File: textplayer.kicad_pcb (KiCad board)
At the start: 2 copper layers, 46 parts, among them J1 ISP, J2 EXT, J3 SERIAL, J4 JTAG, SW1 SW_SPST, SW2 SW_SPST, SW3 SW_SPST, SW4 SW_SPST, SW5 SW_SPST, SW6 SW_SPST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

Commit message: placing...
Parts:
- moved R13 118.4 mm to (51.8, 46.1), turned to 90 degrees
- moved R12 98.6 mm to (51.6, 52.4), turned to 270 degrees
- moved R2 94.6 mm to (80.0, 33.6), turned to 270 degrees
- moved R1 94.5 mm to (82.3, 44.5)
- moved R11 93.8 mm to (52.0, 66.9), turned to 270 degrees
- moved C10 93.4 mm to (57.0, 65.5), turned to 180 degrees
- moved C3 88.9 mm to (68.5, 48.8), turned to 270 degrees
- moved SW6 79.4 mm to (127.5, 64.2)
- moved SW3 69.0 mm to (100.5, 73.2)
- moved R3 65.7 mm to (98.2, 56.6), turned to 270 degrees
- moved SW4 60.8 mm to (117.5, 73.3)
- moved R17 58.6 mm to (57.3, 39.5), turned to 270 degrees
- moved SW1 57.3 mm to (109.1, 64.5)
- moved SW2 56.1 mm to (109.3, 82.7)
- moved R16 55.6 mm to (60.8, 39.5), turned to 270 degrees
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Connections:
- U6 pad 48: (no net) -> +3V3
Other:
- board outline added: 100 x 70 mm

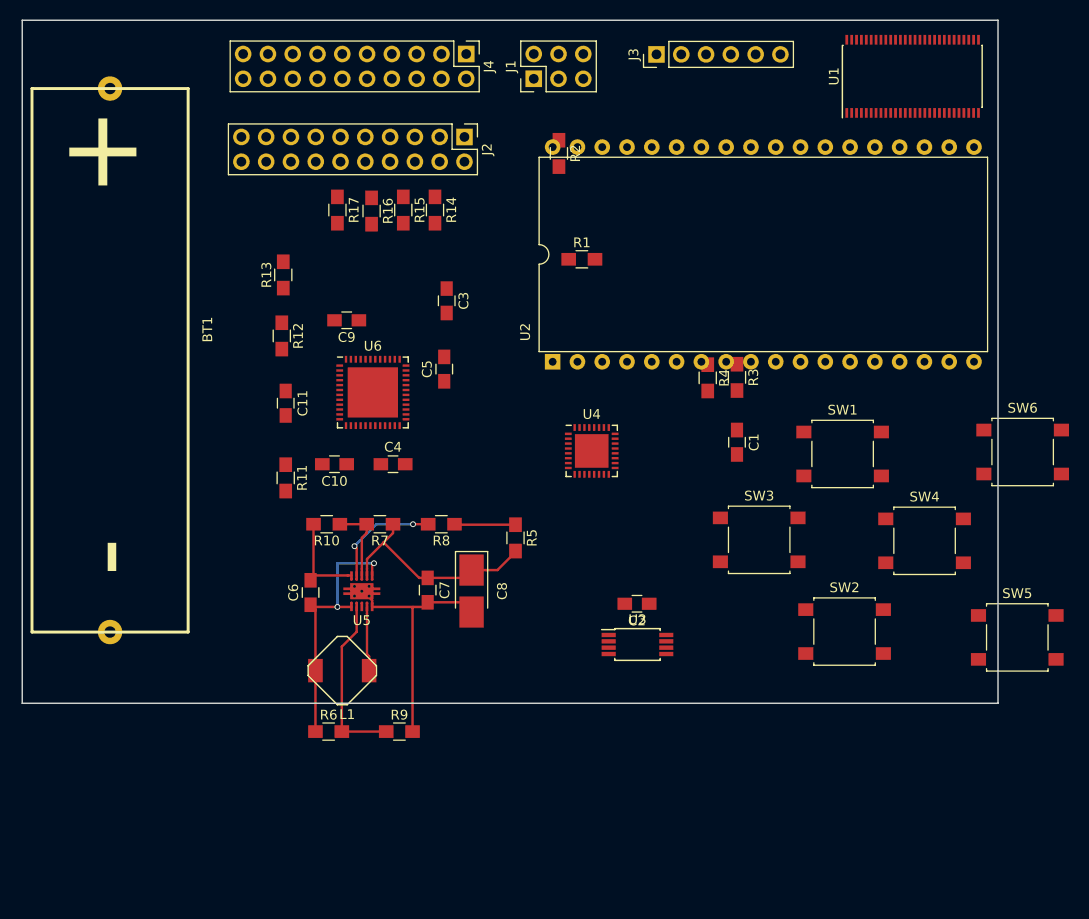
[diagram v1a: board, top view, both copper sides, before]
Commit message: displays schematic ausgelagert
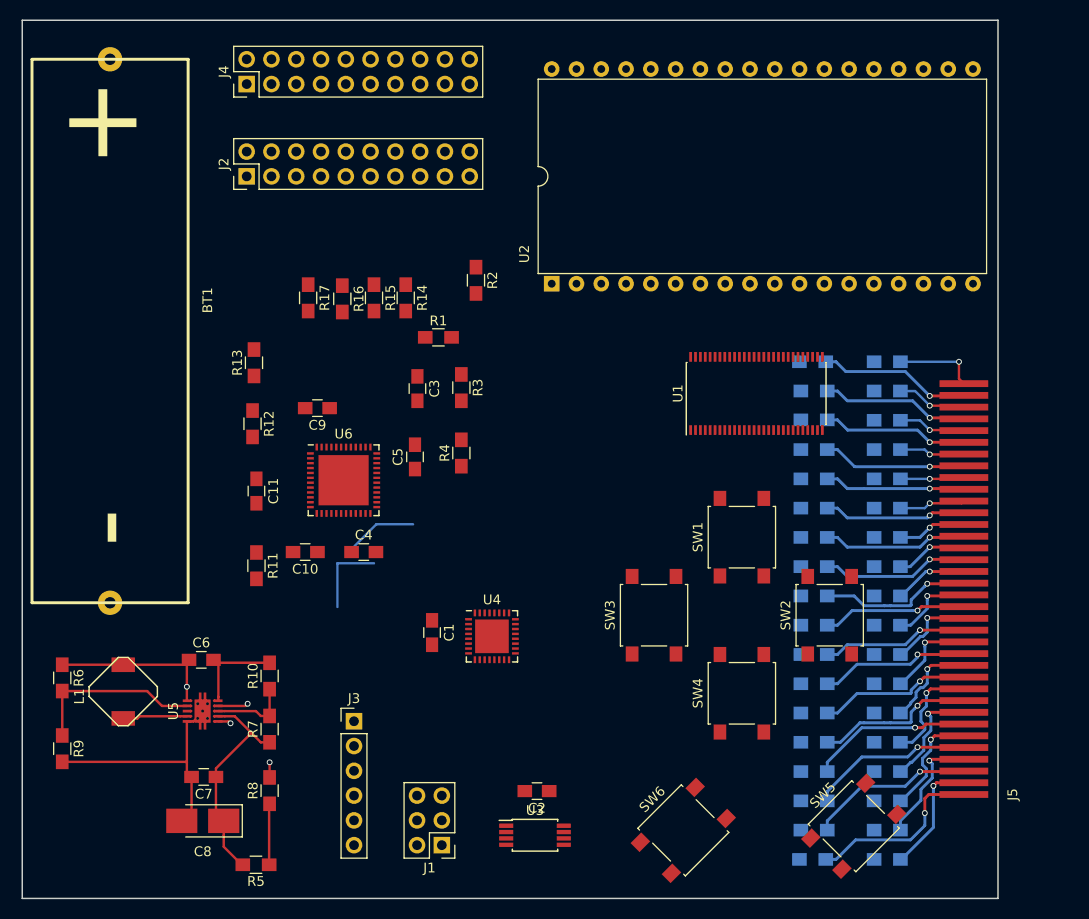
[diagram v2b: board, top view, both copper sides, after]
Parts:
- added J5: TI-30-LCD, Morn_SMD:TI-30-LCD, F.Cu at (121.5, 99.3)
- added R18: DNP, Resistors_SMD:R_0805_HandSoldering, B.Cu at (106.0, 106.0)
- added R19: DNP, Resistors_SMD:R_0805_HandSoldering, B.Cu at (113.7, 106.0)
- added R20: DNP, Resistors_SMD:R_0805_HandSoldering, B.Cu at (106.2, 103.0)
- added R21: DNP, Resistors_SMD:R_0805_HandSoldering, B.Cu at (113.7, 103.0)
- added R22: DNP, Resistors_SMD:R_0805_HandSoldering, B.Cu at (106.2, 100.0)
- added R23: DNP, Resistors_SMD:R_0805_HandSoldering, B.Cu at (113.7, 100.0)
- added R24: DNP, Resistors_SMD:R_0805_HandSoldering, B.Cu at (106.2, 97.0)
- added R25: DNP, Resistors_SMD:R_0805_HandSoldering, B.Cu at (113.7, 97.0)
- added R26: DNP, Resistors_SMD:R_0805_HandSoldering, B.Cu at (106.2, 94.0)
- added R27: DNP, Resistors_SMD:R_0805_HandSoldering, B.Cu at (113.7, 94.0)
- added R28: DNP, Resistors_SMD:R_0805_HandSoldering, B.Cu at (106.2, 91.0)
- added R29: DNP, Resistors_SMD:R_0805_HandSoldering, B.Cu at (113.7, 91.0)
- added R30: DNP, Resistors_SMD:R_0805_HandSoldering, B.Cu at (106.2, 88.0)
- added R31: DNP, Resistors_SMD:R_0805_HandSoldering, B.Cu at (113.7, 88.0)
- added R32: DNP, Resistors_SMD:R_0805_HandSoldering, B.Cu at (106.2, 85.0)
- added R33: DNP, Resistors_SMD:R_0805_HandSoldering, B.Cu at (113.7, 85.0)
- added R34: DNP, Resistors_SMD:R_0805_HandSoldering, B.Cu at (106.2, 82.0)
- added R35: DNP, Resistors_SMD:R_0805_HandSoldering, B.Cu at (113.7, 82.0)
- added R36: DNP, Resistors_SMD:R_0805_HandSoldering, B.Cu at (106.2, 79.0)
- added R37: DNP, Resistors_SMD:R_0805_HandSoldering, B.Cu at (113.7, 79.0)
- added R38: DNP, Resistors_SMD:R_0805_HandSoldering, B.Cu at (106.2, 76.0)
- added R39: DNP, Resistors_SMD:R_0805_HandSoldering, B.Cu at (113.7, 76.0)
- added R40: DNP, Resistors_SMD:R_0805_HandSoldering, B.Cu at (106.2, 73.0)
- added R41: DNP, Resistors_SMD:R_0805_HandSoldering, B.Cu at (113.7, 73.0)
- added R42: DNP, Resistors_SMD:R_0805_HandSoldering, B.Cu at (106.2, 70.0)
- added R43: DNP, Resistors_SMD:R_0805_HandSoldering, B.Cu at (113.7, 70.0)
- added R44: DNP, Resistors_SMD:R_0805_HandSoldering, B.Cu at (106.2, 67.0)
- added R45: DNP, Resistors_SMD:R_0805_HandSoldering, B.Cu at (113.7, 67.0)
- added R46: DNP, Resistors_SMD:R_0805_HandSoldering, B.Cu at (106.2, 64.0)
- added R47: DNP, Resistors_SMD:R_0805_HandSoldering, B.Cu at (113.7, 64.0)
- added R48: DNP, Resistors_SMD:R_0805_HandSoldering, B.Cu at (106.2, 61.0)
- added R49: DNP, Resistors_SMD:R_0805_HandSoldering, B.Cu at (113.7, 61.0)
- added R50: DNP, Resistors_SMD:R_0805_HandSoldering, B.Cu at (106.2, 58.0)
- added R51: DNP, Resistors_SMD:R_0805_HandSoldering, B.Cu at (113.7, 58.0)
- added R52: DNP, Resistors_SMD:R_0805_HandSoldering, B.Cu at (106.0, 55.0)
- added R53: DNP, Resistors_SMD:R_0805_HandSoldering, B.Cu at (113.7, 55.0)
- moved J1 79.1 mm to (68.0, 104.5), turned to 180 degrees
- moved J3 75.0 mm to (59.0, 91.8), turned to 0 degrees
- moved SW6 52.1 mm to (92.8, 103.0), turned to 45 degrees
- moved R5 42.8 mm to (49.0, 106.5), turned to 180 degrees
- moved C1 36.8 mm to (67.0, 82.8)
- moved C8 36.2 mm to (43.5, 102.0), turned to 180 degrees
- moved U1 36.2 mm to (100.2, 58.2)
- moved R9 34.6 mm to (29.1, 94.7), turned to 270 degrees
- moved R8 32.5 mm to (50.4, 99.0), turned to 90 degrees
- moved C7 29.9 mm to (43.6, 97.5), turned to 180 degrees
- moved R3 28.3 mm to (70.0, 57.6)
- moved R6 27.8 mm to (29.1, 87.4), turned to 270 degrees
- moved R4 26.4 mm to (70.0, 64.3), turned to 90 degrees
- moved SW5 25.6 mm to (110.2, 102.6), turned to 45 degrees
- moved SW4 24.4 mm to (98.8, 89.0), turned to 90 degrees
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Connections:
- net /BP0 renamed /Displays/BP0
- net /BP1 renamed /Displays/BP1
- net /BP2 renamed /Displays/BP2
- net /BP3 renamed /Displays/BP3
- J1 pad 5: /RESET -> /AVR_RESET
- U4 pad 11: /RESET -> /AVR_RESET
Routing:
- net Net-(J5-Pad1): track 0.00 -> 18.5 mm, vias 0 -> 1
- net Net-(J5-Pad3): track 0.00 -> 17.1 mm, vias 0 -> 1
- net Net-(J5-Pad5): track 0.00 -> 16.8 mm, vias 0 -> 1
- net Net-(J5-Pad7): track 0.00 -> 16.6 mm, vias 0 -> 1
- net Net-(J5-Pad9): track 0.00 -> 16.4 mm, vias 0 -> 1
- net Net-(J5-Pad11): track 0.00 -> 15.7 mm, vias 0 -> 1
- net Net-(J5-Pad19): track 0.00 -> 15.7 mm, vias 0 -> 1
- net Net-(J5-Pad35): track 0.00 -> 15.6 mm, vias 0 -> 1
- net Net-(J5-Pad13): track 0.00 -> 15.4 mm, vias 0 -> 1
- net Net-(J5-Pad33): track 0.00 -> 15.2 mm, vias 0 -> 1
- net Net-(J5-Pad21): track 0.00 -> 15.2 mm, vias 0 -> 1
- net Net-(J5-Pad15): track 0.00 -> 15.0 mm, vias 0 -> 1
- net Net-(J5-Pad31): track 0.00 -> 15.0 mm, vias 0 -> 1
- net Net-(J5-Pad23): track 0.00 -> 14.9 mm, vias 0 -> 1
- net Net-(J5-Pad17): track 0.00 -> 14.8 mm, vias 0 -> 1
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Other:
- board size 100 x 70 mm -> 100 x 90 mm

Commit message: place should be done now
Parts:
- added J10: GND, Measurement_Points:Measurement_Point_Round-TH_Small, F.Cu at (62.0, 102.0)
- added J11: GND, Measurement_Points:Measurement_Point_Round-SMD-Pad_Big, F.Cu at (62.0, 107.0)
- added J12: VCC, Measurement_Points:Measurement_Point_Round-TH_Small, F.Cu at (55.0, 102.0)
- added J13: VCC, Measurement_Points:Measurement_Point_Round-SMD-Pad_Big, F.Cu at (55.0, 107.0)
- added J6: BP0, Measurement_Points:Measurement_Point_Square-SMD-Pad_Small, B.Cu at (99.0, 57.8)
- added J7: BP2, Measurement_Points:Measurement_Point_Square-SMD-Pad_Small, B.Cu at (99.0, 54.8)
- added J8: BP1, Measurement_Points:Measurement_Point_Square-SMD-Pad_Small, B.Cu at (99.0, 60.8)
- added J9: BP3, Measurement_Points:Measurement_Point_Square-SMD-Pad_Small, B.Cu at (99.0, 63.8)
- moved BT1 53.6 mm to (35.1, 26.1), turned to 270 degrees
- moved R2 40.6 mm to (78.2, 86.8), turned to 180 degrees
- moved R3 33.4 mm to (78.2, 90.0), turned to 180 degrees
- moved R1 32.7 mm to (78.2, 83.5)
- moved R4 30.3 mm to (78.2, 93.5), turned to 180 degrees
- moved C1 27.6 mm to (90.0, 67.5), turned to 0 degrees
- moved R11 27.6 mm to (48.0, 48.4)
- moved R12 26.8 mm to (72.0, 48.4)
- moved C3 25.6 mm to (78.2, 80.0), turned to 0 degrees
- moved U1 13.4 mm to (86.9, 59.8), turned to 270 degrees
- moved U4 9.85 mm to (74.4, 73.4)
- moved J1 8.68 mm to (69.5, 96.0)
- moved J3 8.60 mm to (60.0, 83.3)
- moved R13 7.49 mm to (52.0, 48.4)
- moved R15 6.95 mm to (68.0, 48.4)
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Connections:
- R1 pad 2: Net-(R1-Pad2) -> /SDA
- U1 pad 10: Net-(U1-Pad10) -> /Displays/5L
- U1 pad 11: Net-(U1-Pad11) -> /Displays/5E
- U1 pad 13: Net-(U1-Pad13) -> /Displays/8D
- U1 pad 14: Net-(U1-Pad14) -> /Displays/8M
- U1 pad 15: Net-(U1-Pad15) -> /Displays/7D
- U1 pad 16: Net-(U1-Pad16) -> /Displays/7M
- U1 pad 17: Net-(U1-Pad17) -> /Displays/6D
- U1 pad 18: Net-(U1-Pad18) -> /Displays/6M
- U1 pad 19: Net-(U1-Pad19) -> /Displays/5D
- U1 pad 20: Net-(U1-Pad20) -> /Displays/5M
- U1 pad 21: Net-(U1-Pad21) -> /Displays/4D
- U1 pad 22: Net-(U1-Pad22) -> /Displays/4M
- U1 pad 23: Net-(U1-Pad23) -> /Displays/3D
- U1 pad 24: Net-(U1-Pad24) -> /Displays/3M
- U1 pad 25: Net-(U1-Pad25) -> /Displays/2D
- U1 pad 26: Net-(U1-Pad26) -> /Displays/2M
- U1 pad 27: Net-(U1-Pad27) -> /Displays/1D
- U1 pad 28: Net-(U1-Pad28) -> /Displays/1M
- U1 pad 29: Net-(U1-Pad29) -> /Displays/1E
- U1 pad 30: Net-(U1-Pad30) -> /Displays/1L
- U1 pad 31: Net-(U1-Pad31) -> /Displays/2E
- U1 pad 32: Net-(U1-Pad32) -> /Displays/2L
- U1 pad 33: Net-(U1-Pad33) -> /Displays/3E
- U1 pad 34: Net-(U1-Pad34) -> /Displays/3L
- U1 pad 35: Net-(U1-Pad35) -> /Displays/4E
- U1 pad 36: Net-(U1-Pad36) -> /Displays/4L
- U1 pad 4: Net-(U1-Pad4) -> /Displays/8L
- U1 pad 5: Net-(U1-Pad5) -> /Displays/8E
- U1 pad 6: Net-(U1-Pad6) -> /Displays/7L
- U1 pad 7: Net-(U1-Pad7) -> /Displays/7E
- U1 pad 8: Net-(U1-Pad8) -> /Displays/6L
- U1 pad 9: Net-(U1-Pad9) -> /Displays/6E
- U2 pad 1: Net-(U2-Pad1) -> /Displays/1E
- U2 pad 10: Net-(U2-Pad10) -> /Displays/5L
- U2 pad 11: Net-(U2-Pad11) -> /Displays/6E
- U2 pad 12: Net-(U2-Pad12) -> /Displays/6L
- U2 pad 13: Net-(U2-Pad13) -> /Displays/7E
- U2 pad 14: Net-(U2-Pad14) -> /Displays/7L
- U2 pad 15: Net-(U2-Pad15) -> /Displays/8E
- U2 pad 16: Net-(U2-Pad16) -> /Displays/8L
- U2 pad 2: Net-(U2-Pad2) -> /Displays/1L
- U2 pad 21: Net-(U2-Pad21) -> /Displays/8D
- U2 pad 22: Net-(U2-Pad22) -> /Displays/8M
- U2 pad 23: Net-(U2-Pad23) -> /Displays/7D
- U2 pad 24: Net-(U2-Pad24) -> /Displays/7M
- U2 pad 25: Net-(U2-Pad25) -> /Displays/6D
- U2 pad 26: Net-(U2-Pad26) -> /Displays/6M
- U2 pad 27: Net-(U2-Pad27) -> /Displays/5D
- U2 pad 28: Net-(U2-Pad28) -> /Displays/5M
- U2 pad 29: Net-(U2-Pad29) -> /Displays/4D
- U2 pad 3: Net-(U2-Pad3) -> /Displays/2E
- U2 pad 30: Net-(U2-Pad30) -> /Displays/4M
- U2 pad 31: Net-(U2-Pad31) -> /Displays/3D
- U2 pad 32: Net-(U2-Pad32) -> /Displays/3M
- U2 pad 33: Net-(U2-Pad33) -> /Displays/2D
- U2 pad 34: Net-(U2-Pad34) -> /Displays/2M
- U2 pad 35: Net-(U2-Pad35) -> /Displays/1D
- U2 pad 36: Net-(U2-Pad36) -> /Displays/1M
- U2 pad 4: Net-(U2-Pad4) -> /Displays/2L
- U2 pad 5: Net-(U2-Pad5) -> /Displays/3E
- U2 pad 6: Net-(U2-Pad6) -> /Displays/3L
- U2 pad 7: Net-(U2-Pad7) -> /Displays/4E
- U2 pad 8: Net-(U2-Pad8) -> /Displays/4L
- U2 pad 9: Net-(U2-Pad9) -> /Displays/5E
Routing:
- net +3V3: track 6.27 -> 99.3 mm
- net GND: track 35.5 -> 95.2 mm
- net /Displays/8D: track 0.00 -> 53.4 mm
- net /Displays/BP2: track 0.00 -> 51.7 mm
- net /Displays/8M: track 0.00 -> 51.5 mm
- net /Displays/BP3: track 0.00 -> 50.3 mm
- net /Displays/7D: track 0.00 -> 49.5 mm
- net /Displays/7M: track 0.00 -> 47.5 mm
- net /Displays/6D: track 0.00 -> 45.6 mm
- net /Displays/6M: track 0.00 -> 43.6 mm
- net /Displays/5D: track 0.00 -> 41.7 mm
- net /Displays/5M: track 0.00 -> 39.7 mm
- net /Displays/4D: track 0.00 -> 37.7 mm
- net /Displays/4M: track 0.00 -> 35.8 mm
- net /Displays/3D: track 0.00 -> 34.9 mm
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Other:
- outline, holes or cut-outs redrawn

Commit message: routing...
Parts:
- moved C9 1.75 mm to (55.2, 58.0)
- moved C5 1.50 mm to (67.2, 64.8)
- turned U4 to 90 degrees
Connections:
- R18 pad 2: Net-(R18-Pad2) -> /Displays/1L
- R19 pad 2: Net-(R19-Pad2) -> /Displays/1E
- R20 pad 2: Net-(R20-Pad2) -> /Displays/2L
- R21 pad 2: Net-(R21-Pad2) -> /Displays/2E
- R22 pad 2: Net-(R22-Pad2) -> /Displays/3L
- R23 pad 2: Net-(R23-Pad2) -> /Displays/3E
- R24 pad 2: Net-(R24-Pad2) -> /Displays/4L
- R25 pad 2: Net-(R25-Pad2) -> /Displays/4E
- R26 pad 2: Net-(R26-Pad2) -> /Displays/X1
- R27 pad 2: Net-(R27-Pad2) -> /Displays/X2
- R28 pad 2: Net-(R28-Pad2) -> /Displays/X3
- R29 pad 2: Net-(R29-Pad2) -> /Displays/X4
- R30 pad 2: Net-(R30-Pad2) -> /Displays/X5
- R31 pad 2: Net-(R31-Pad2) -> /Displays/X6
- R32 pad 2: Net-(R32-Pad2) -> /Displays/X7
- R33 pad 2: Net-(R33-Pad2) -> /Displays/1M
- R34 pad 2: Net-(R34-Pad2) -> /Displays/1D
- R35 pad 2: Net-(R35-Pad2) -> /Displays/2M
- R36 pad 2: Net-(R36-Pad2) -> /Displays/2D
- R37 pad 2: Net-(R37-Pad2) -> /Displays/3M
- R38 pad 2: Net-(R38-Pad2) -> /Displays/3D
- R39 pad 2: Net-(R39-Pad2) -> /Displays/4M
- R40 pad 2: Net-(R40-Pad2) -> /Displays/4D
- R41 pad 2: Net-(R41-Pad2) -> /Displays/5M
- R42 pad 2: Net-(R42-Pad2) -> /Displays/5D
- R43 pad 2: Net-(R43-Pad2) -> /Displays/6M
- R44 pad 2: Net-(R44-Pad2) -> /Displays/6D
- R45 pad 2: Net-(R45-Pad2) -> /Displays/7M
- R46 pad 2: Net-(R46-Pad2) -> /Displays/7D
- R47 pad 2: Net-(R47-Pad2) -> /Displays/8M
- R48 pad 2: Net-(R48-Pad2) -> /Displays/8D
- R49 pad 2: Net-(R49-Pad2) -> /Displays/X8
- R50 pad 2: Net-(R50-Pad2) -> /Displays/5E
- R51 pad 2: Net-(R51-Pad2) -> /Displays/5L
- R52 pad 2: Net-(R52-Pad2) -> /Displays/6E
- R53 pad 2: Net-(R53-Pad2) -> /Displays/6L
- U1 pad 12: Net-(U1-Pad12) -> /Displays/X8
- U1 pad 37: Net-(U1-Pad37) -> /Displays/X1
- U1 pad 38: Net-(U1-Pad38) -> /Displays/X2
- U1 pad 39: Net-(U1-Pad39) -> /Displays/X3
- U1 pad 40: Net-(U1-Pad40) -> /Displays/X4
- U1 pad 41: Net-(U1-Pad41) -> /Displays/X5
- U1 pad 42: Net-(U1-Pad42) -> /Displays/X6
- U1 pad 43: Net-(U1-Pad43) -> /Displays/X7
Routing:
- net +3V3: track 99.3 -> 198.9 mm, vias 0 -> 3
- net /Displays/5M: track 39.7 -> 128.6 mm, vias 0 -> 3
- net /Displays/5D: track 41.7 -> 128.2 mm, vias 0 -> 3
- net GND: track 95.2 -> 166.0 mm, vias 0 -> 2
- net /Displays/1E: track 17.9 -> 84.0 mm
- net /Displays/6M: track 43.6 -> 108.4 mm, vias 0 -> 3
- net /Displays/2E: track 17.0 -> 79.2 mm
- net /Displays/3E: track 18.7 -> 79.2 mm, vias 1 -> 3
- net /Displays/4E: track 20.3 -> 76.8 mm, vias 1 -> 3
- net /Displays/1L: track 17.1 -> 73.2 mm
- net /Displays/6D: track 45.6 -> 101.4 mm, vias 0 -> 3
- net /Displays/2L: track 17.8 -> 71.7 mm
- net /Displays/7M: track 47.5 -> 100.0 mm, vias 0 -> 3
- net /Displays/1M: track 34.0 -> 84.5 mm, vias 0 -> 1
- net /Displays/3L: track 19.7 -> 69.3 mm
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
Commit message: more routing...
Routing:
- net /SDA: track 44.5 -> 153.7 mm, vias 2 -> 5
- net /RESET: track 0.00 -> 94.4 mm, vias 0 -> 2
- net /SCL: track 42.5 -> 131.9 mm, vias 2 -> 5
- net /E6: track 0.00 -> 61.6 mm, vias 0 -> 4
- net +3V3: track 198.9 -> 257.5 mm
- net /E8: track 0.00 -> 56.4 mm, vias 0 -> 4
- net /TMS: track 0.00 -> 55.8 mm, vias 0 -> 4
- net /TCK: track 0.00 -> 54.4 mm, vias 0 -> 2
- net /E7: track 0.00 -> 54.2 mm, vias 0 -> 4
- net Net-(J3-Pad5): track 11.3 -> 63.2 mm, vias 2 -> 4
- net /TDI: track 0.00 -> 47.4 mm, vias 0 -> 2
- net /TDO: track 0.00 -> 45.7 mm, vias 0 -> 1
- net /nTRST: track 0.00 -> 45.3 mm, vias 0 -> 2
- net /RXD: track 0.00 -> 42.5 mm, vias 0 -> 2
- net /E5: track 0.00 -> 41.5 mm, vias 0 -> 4
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
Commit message: 5 unconnected
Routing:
- net GND: track 181.2 -> 601.4 mm, vias 2 -> 16
- net /SW_A: track 0.00 -> 170.2 mm, vias 0 -> 5
- net /SW_DN: track 0.00 -> 136.2 mm, vias 0 -> 5
- net /SW_UP: track 0.00 -> 131.1 mm, vias 0 -> 5
- net /SW_B: track 0.00 -> 114.2 mm, vias 0 -> 3
- net /SW_RI: track 0.00 -> 112.6 mm, vias 0 -> 5
- net /SW_LF: track 0.00 -> 99.3 mm, vias 0 -> 5
- net +3V3: track 257.5 -> 345.4 mm, vias 3 -> 10
- net /E10: track 0.00 -> 83.8 mm, vias 0 -> 3
- net /E15: track 0.00 -> 78.9 mm, vias 0 -> 2
- net /E13: track 0.00 -> 77.7 mm, vias 0 -> 2
- net /E18: track 0.00 -> 76.4 mm, vias 0 -> 2
- net /E17: track 0.00 -> 75.4 mm, vias 0 -> 2
- net /E12: track 0.00 -> 75.3 mm, vias 0 -> 2
- net /DTR: track 0.00 -> 74.3 mm, vias 0 -> 2
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
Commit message: almost done..
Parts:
- added D1: LED, LEDs:LED_0805, F.Cu at (67.8, 105.3)
- added R54: R, Resistors_SMD:R_0805_HandSoldering, F.Cu at (67.8, 100.7)
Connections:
- J6 pad 1: Net-(J6-Pad1) -> /Displays/BP0
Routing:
- net GND: track 601.4 -> 613.6 mm, vias 16 -> 20
- net Net-(BT1-Pad1): track 23.3 -> 33.7 mm, vias 0 -> 2
- net /Displays/BP0: track 32.4 -> 40.7 mm, vias 1 -> 2
- net /SW_UP: track 131.1 -> 135.1 mm
- net +3V3: track 345.4 -> 349.1 mm
- net Net-(D1-Pad2): track 0.00 -> 2.20 mm
- net /SW_A: vias 5 -> 7
- added copper zone on B.Cu, net GND
- added copper zone on F.Cu, net GND

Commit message: werde es jetzt gleich absenden
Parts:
- moved J2 2.00 mm to (46.0, 36.0)
- moved J4 2.00 mm to (46.0, 26.5)
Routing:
- net /E10: track 83.8 -> 99.2 mm, vias 3 -> 4
- net /E15: track 78.9 -> 86.1 mm, vias 2 -> 1
- net /TDO: track 45.6 -> 41.0 mm, vias 1 -> 2
- net GND: track 613.6 -> 617.2 mm, vias 20 -> 29
- net /E16: track 71.6 -> 68.2 mm, vias 2 -> 1
- net /E14: track 65.3 -> 62.4 mm, vias 2 -> 1
- net /SW_UP: track 135.1 -> 132.6 mm
- net /DTR: track 74.3 -> 72.0 mm
- net /E18: track 76.4 -> 74.2 mm, vias 2 -> 1
- net /E13: track 77.7 -> 75.7 mm, vias 2 -> 1
- net /SDA: track 165.4 -> 167.4 mm
- net /SCL: track 133.6 -> 135.6 mm
- net /E9: track 65.6 -> 63.8 mm
- net /TMS: track 56.1 -> 57.7 mm
- net /E12: track 75.3 -> 73.7 mm, vias 2 -> 1
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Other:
- board text added: "1"
- board text added: "10"
- board text added: "11"
- board text added: "12"
- board text added: "13"
- board text added: "14"
- board text added: "15"
- board text added: "16"
- board text added: "17"
- board text added: "18"
- board text added: "19"
- board text added: "2"
- board text added: "20"
- board text added: "21"
- board text added: "22"
- board text added: "23"
- board text added: "24"
- board text added: "25"
- board text added: "26"
- board text added: "27"
- board text added: "28"
- board text added: "29"
- board text added: "3"
- board text added: "3.3V"
- board text added: "30"
- board text added: "32"
- board text added: "33"
- board text added: "34"
- board text added: "35"
- board text added: "36"
- board text added: "4"
- board text added: "5"
- board text added: "6"
- board text added: "7"
- board text added: "8"
- board text added: "9"
- board text added: "A"
- board text added: "B"
- board text added: "BP0"
- board text added: "BP1"
- board text added: "BP2"
- board text added: "BP3"
- board text added: "EXT"
- board text added: "GND"
- board text added: "ISP"
- board text added: "JTAG"
- board text added: "SERIAL"
- board text added: "textplayer / Tobias Kaiser / Apr 9 2017"
